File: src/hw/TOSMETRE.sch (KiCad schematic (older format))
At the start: 53 parts, among them J1 Alim, J2 Conn_Coaxial, J3 Conn_01x08_Male, J5 Conn_Coaxial, SW1 SW_Push, SW2 SW_Push_Dual_x2, U1 18F1320, U2 L7805, U3 LT1818, U4 AD5175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

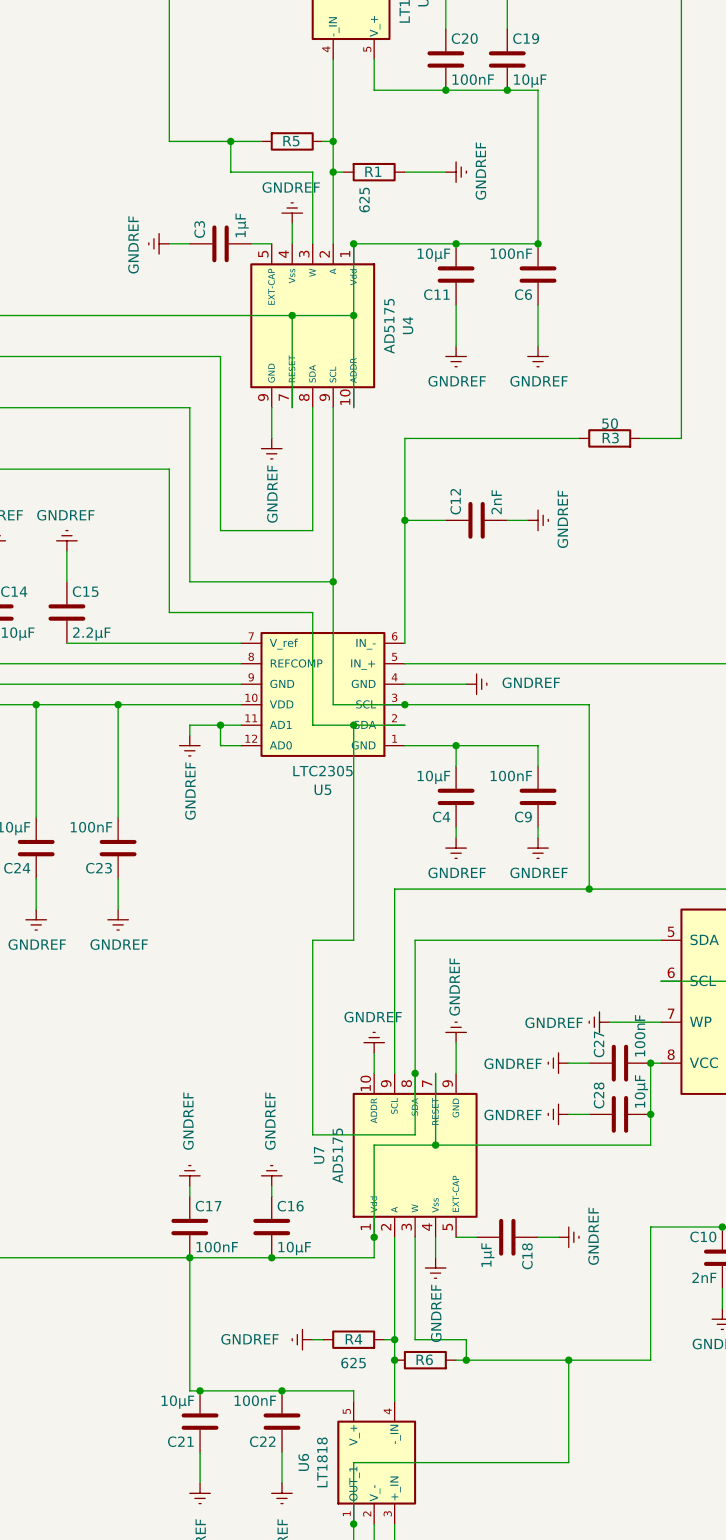
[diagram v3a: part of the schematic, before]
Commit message: #301
Modification valeur R1 et R4 valent 510 ohms (pas 625)
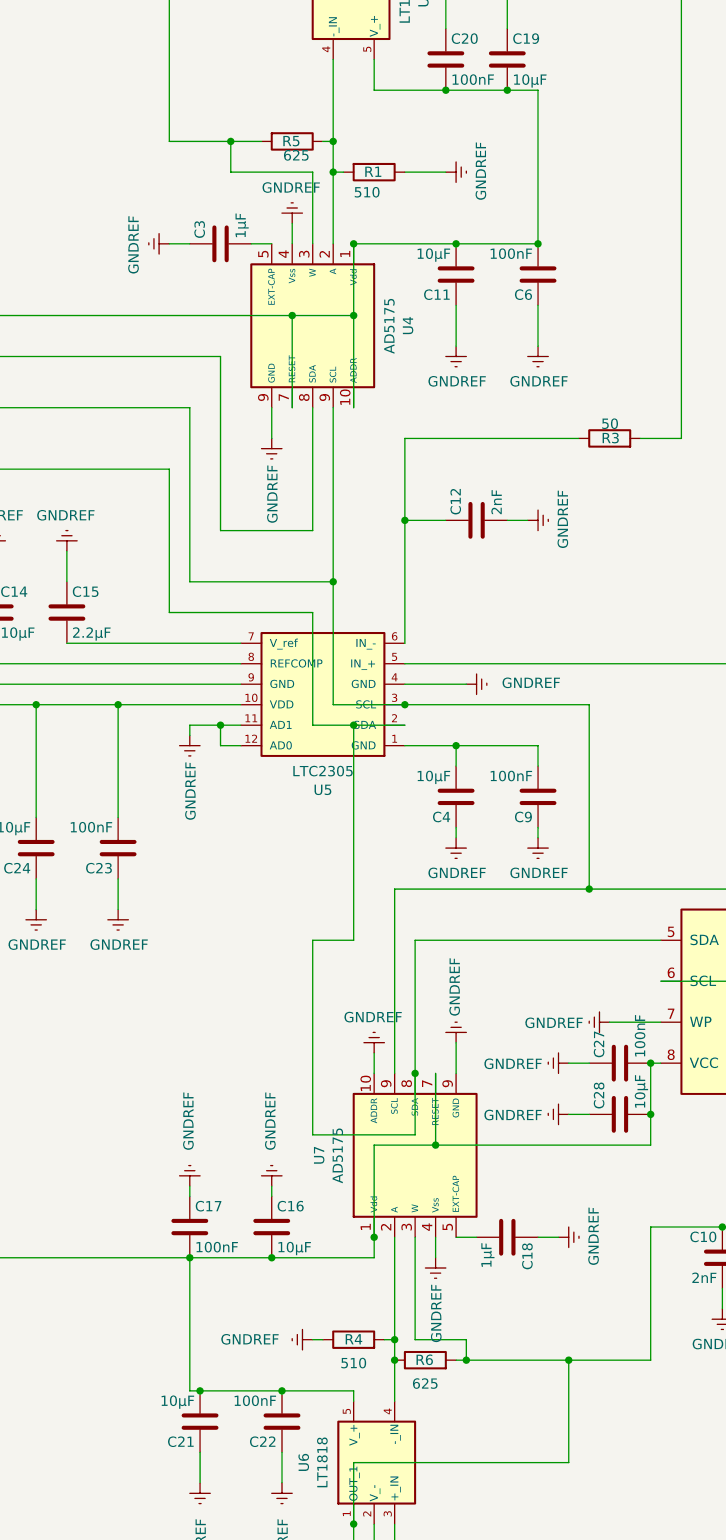
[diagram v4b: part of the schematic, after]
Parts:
- R1, R4: value 625 -> 510
- R5, R6: value (none) -> 625
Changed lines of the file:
@@
 P 9600 3200
 F 0 "R1" V 9600 3150 50  0000 L CNN
-F 1 "625" H 9670 3155 50  0000 L CNN
+F 1 "510" V 9700 3100 50  0000 L CNN
 F 2 "Resistor_SMD:R_1206_3216Metric" V 9530 3200 50  0001 C CNN
 F 3 "~" H 9600 3200 50  0001 C CNN
@@
 P 9200 3050
 F 0 "R5" V 9200 3000 50  0000 L CNN
-F 1 " " H 9270 3005 50  0000 L CNN
+F 1 "625" V 9270 3005 50  0000 L CNN
 F 2 "Resistor_SMD:R_1206_3216Metric" V 9130 3050 50  0001 C CNN
 F 3 "~" H 9200 3050 50  0001 C CNN
@@
 P 9850 9000
 F 0 "R6" V 9850 9050 50  0000 R CNN
-F 1 " " V 9734 9000 50  0000 C CNN
+F 1 "625" V 9734 9000 50  0000 C CNN
 F 2 "Resistor_SMD:R_1206_3216Metric" V 9780 9000 50  0001 C CNN
 F 3 "~" H 9850 9000 50  0001 C CNN
@@
 P 9500 8900
 F 0 "R4" V 9500 8900 50  0000 C CNN
-F 1 "625" V 9384 8900 50  0000 C CNN
+F 1 "510" V 9384 8900 50  0000 C CNN
 F 2 "Resistor_SMD:R_1206_3216Metric" V 9430 8900 50  0001 C CNN
 F 3 "~" H 9500 8900 50  0001 C CNN

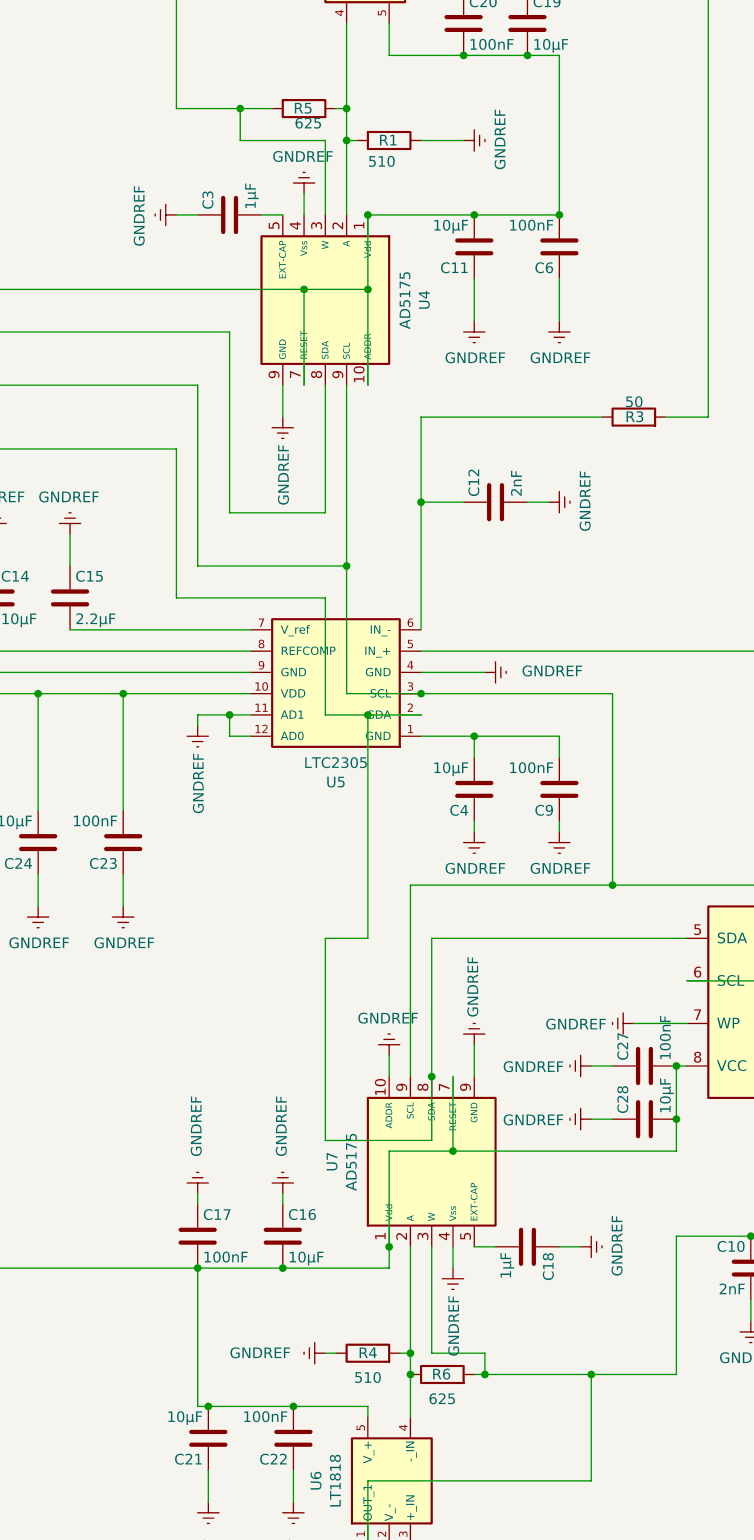
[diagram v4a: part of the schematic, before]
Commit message: #301 modification valeur de R1 et R4
Modification valeur de R1 et R4 en 625

Du coup  valeur de R5 et R6  a verifier
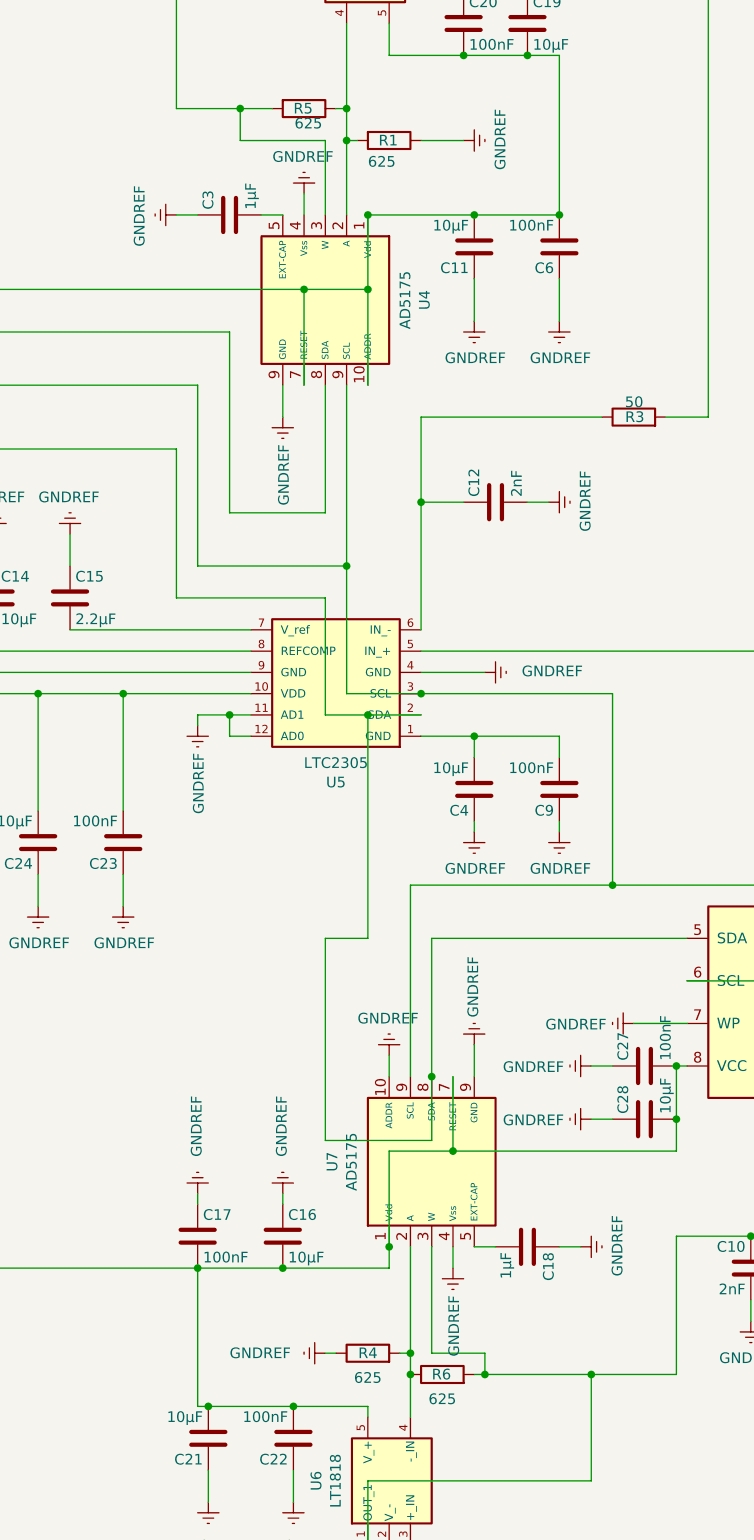
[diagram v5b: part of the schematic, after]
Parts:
- R1, R4: value 510 -> 625
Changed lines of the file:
@@
 P 9600 3200
 F 0 "R1" V 9600 3150 50  0000 L CNN
-F 1 "510" V 9700 3100 50  0000 L CNN
+F 1 "625" V 9700 3100 50  0000 L CNN
 F 2 "Resistor_SMD:R_1206_3216Metric" V 9530 3200 50  0001 C CNN
 F 3 "~" H 9600 3200 50  0001 C CNN
@@
 P 9500 8900
 F 0 "R4" V 9500 8900 50  0000 C CNN
-F 1 "510" V 9384 8900 50  0000 C CNN
+F 1 "625" V 9384 8900 50  0000 C CNN
 F 2 "Resistor_SMD:R_1206_3216Metric" V 9430 8900 50  0001 C CNN
 F 3 "~" H 9500 8900 50  0001 C CNN

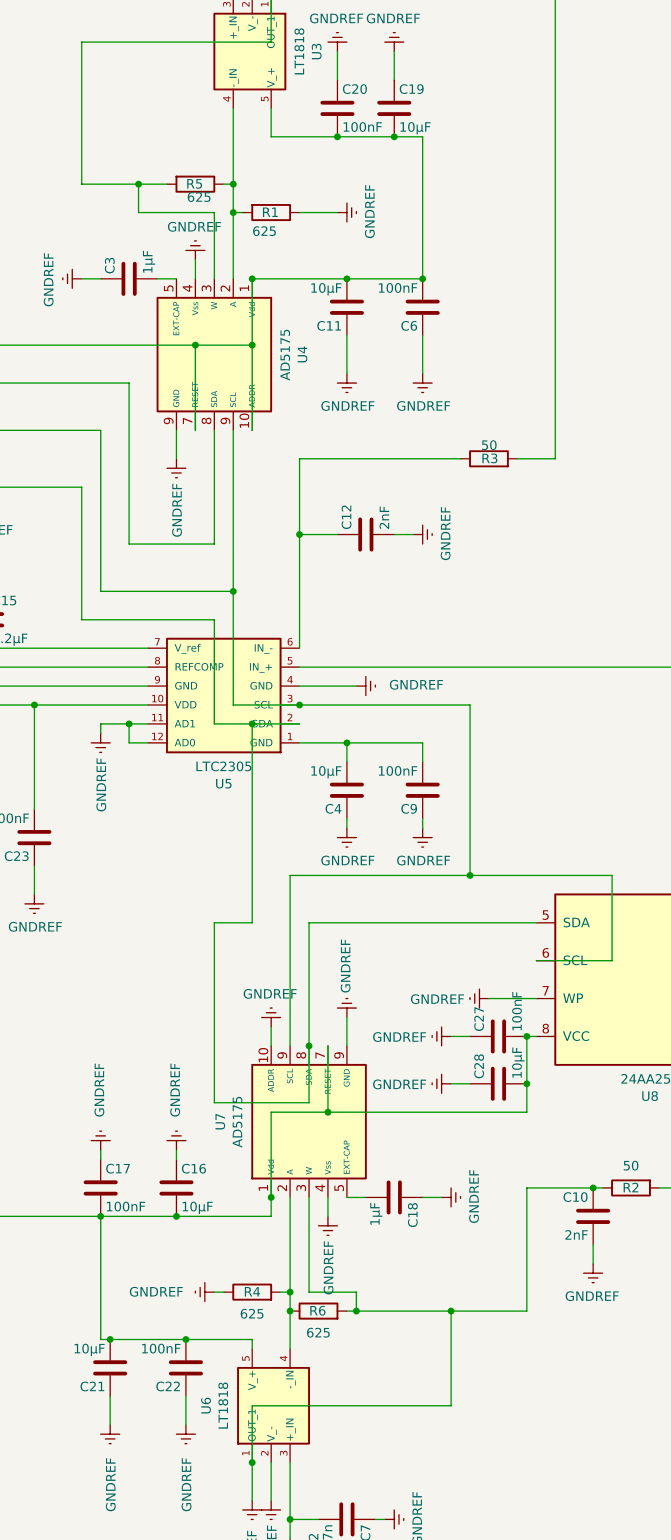
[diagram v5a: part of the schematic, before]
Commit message: #301
Rajout commentaire résistance test ADC1 sur resistance  R6 et R5
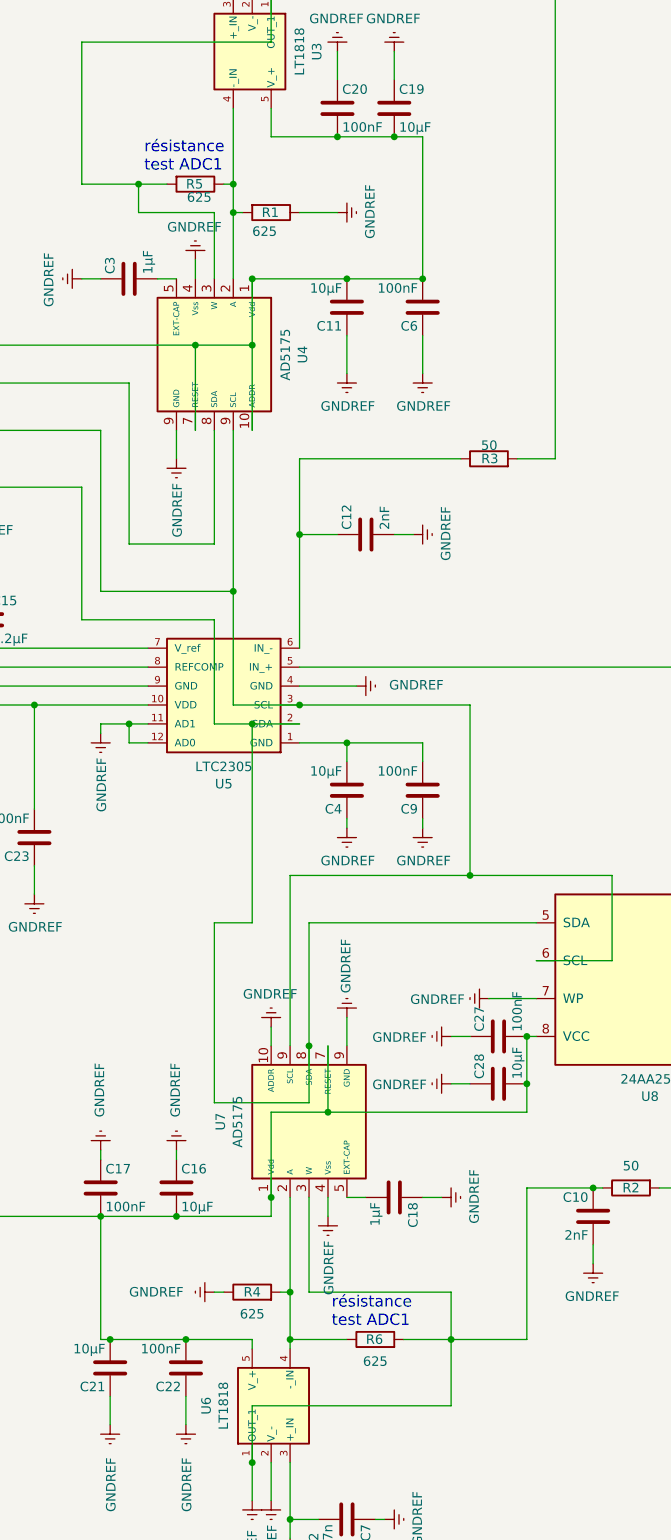
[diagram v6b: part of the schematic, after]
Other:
- note added: "résistance\ntest ADC1\n"
- moved on the sheet: R6
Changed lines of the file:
@@
 	0    1    1    0
-$EndComp
-$Comp
-L Device:R R6
-U 1 1 5ECBB13D
-P 9850 9000
-F 0 "R6" V 9850 9050 50  0000 R CNN
-F 1 "625" V 9734 9000 50  0000 C CNN
-F 2 "Resistor_SMD:R_1206_3216Metric" V 9780 9000 50  0001 C CNN
-F 3 "~" H 9850 9000 50  0001 C CNN
-	1    9850 9000
-	0    -1   -1   0
 $EndComp
 Wire Wire Line
@@
 REF\n
 Wire Wire Line
-	9700 9200 9700 9000
-Wire Wire Line
-	9700 9000 9700 8900
-Connection ~ 9700 9000
-Wire Wire Line
 	9700 8900 9650 8900
 Wire Wire Line
 	9800 8400 9800 8900
-Wire Wire Line
-	9800 8900 10050 8900
-Wire Wire Line
-	10050 8900 10050 9000
-Wire Wire Line
-	10000 9000 10050 9000
-Connection ~ 10050 9000
-Wire Wire Line
-	10050 9000 10550 9000
 Connection ~ 8700 8500
 Wire Wire Line
@@
 	9500 9500 10550 9500
 Wire Wire Line
-	10550 9000 10550 9500
+	10550 9150 10550 9500
 Wire Wire Line
 	9500 9500 9500 9800
@@
 	11350 8350 11300 8350
 Wire Wire Line
-	10550 9000 10950 9000
-Wire Wire Line
-	10950 9000 10950 8350
-Wire Wire Line
 	10950 8350 11300 8350
-Connection ~ 10550 9000
+Connection ~ 10550 9150
 Connection ~ 11300 8350
 Wire Wire Line
@@
 Wire Wire Line
 	10400 6000 10400 6100
+Wire Wire Line
+	10950 8350 10950 9150
+Wire Wire Line
+	10550 8900 10550 9150
+Wire Wire Line
+	9800 8900 10550 8900
+Wire Wire Line
+	10300 9150 10550 9150
+Wire Wire Line
+	9700 8900 9700 9150
+Wire Wire Line
+	10000 9150 9700 9150
+Wire Wire Line
+	10550 9150 10950 9150
+Connection ~ 9700 9150
+Wire Wire Line
+	9700 9150 9700 9200
+$Comp
+L Device:R R6
+U 1 1 5ECBB13D
+P 10150 9150
+F 0 "R6" V 10150 9200 50  0000 R CNN
+F 1 "625" V 10034 9150 50  0000 C CNN
+F 2 "Resistor_SMD:R_1206_3216Metric" V 10080 9150 50  0001 C CNN
+F 3 "~" H 10150 9150 50  0001 C CNN
+	1    10150 9150
+	0    -1   -1   0
+$EndComp
+Text Notes 9920 9090 0    60   ~ 0
+résistance\ntest ADC1\n
+Text Notes 8930 2990 0    60   ~ 0
+résistance\ntest ADC1\n
 $EndSCHEMATC
